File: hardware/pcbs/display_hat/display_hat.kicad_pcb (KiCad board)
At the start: 2 copper layers, 31 x 65 mm, 13 parts, among them J1 WAVESHARE_HAT_HEADER, J2 Header_01x08, J3 Header_01x08, J4 MTA100_02

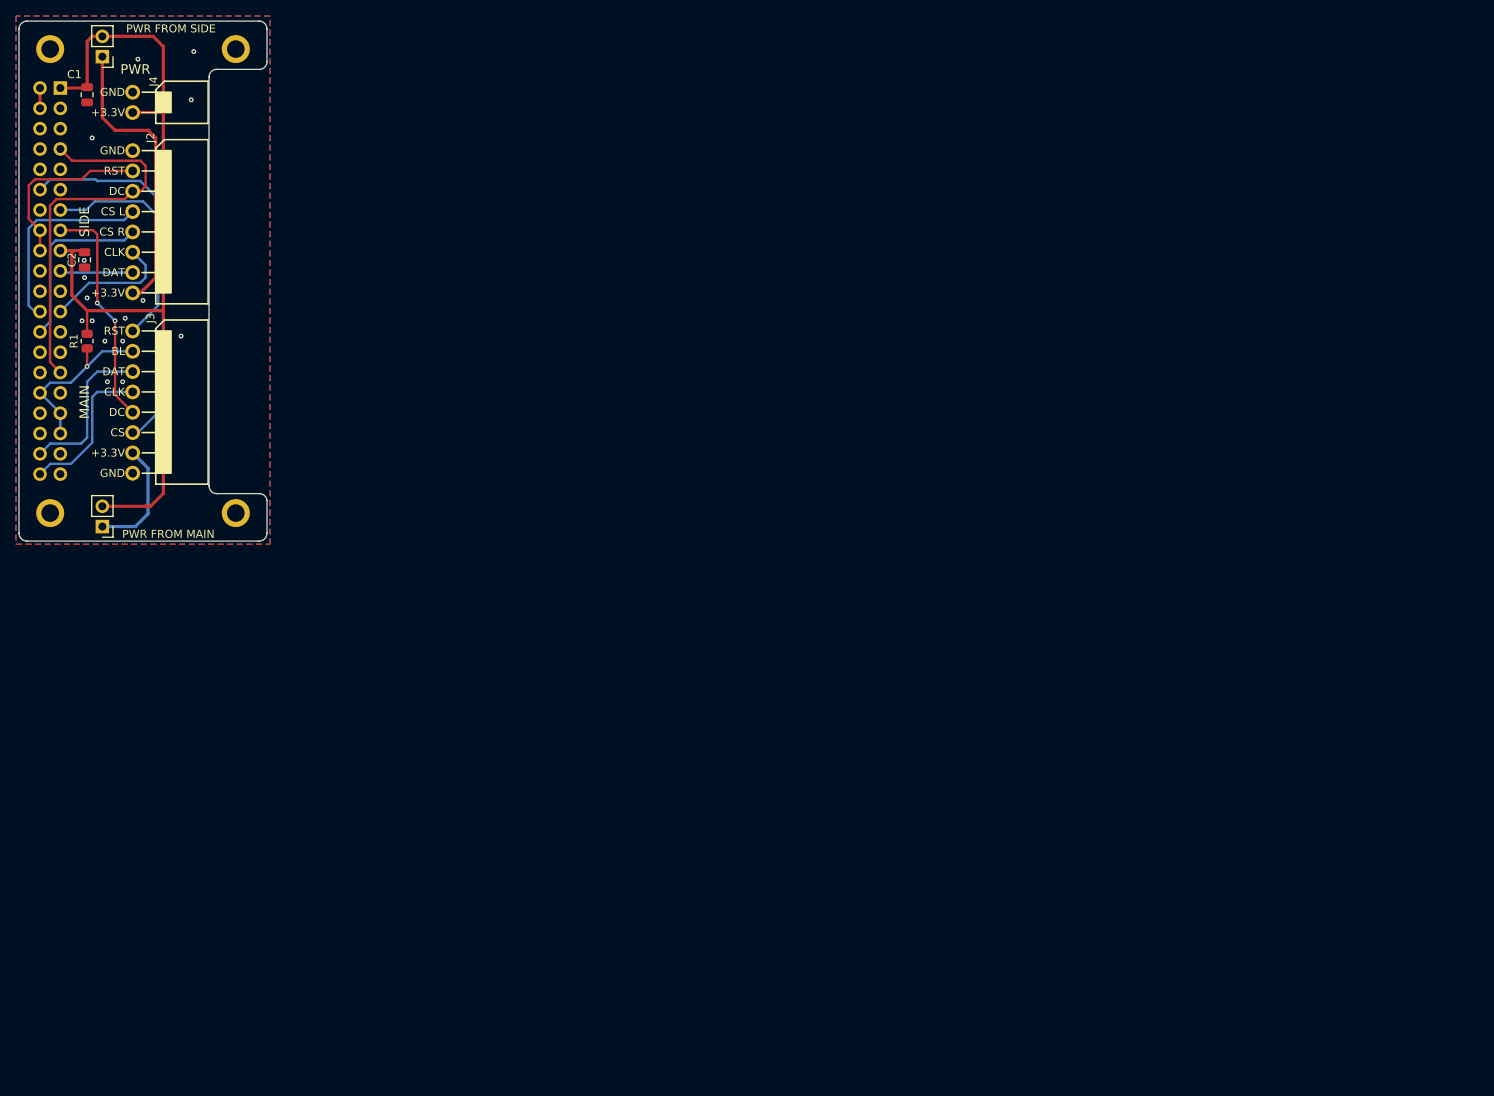
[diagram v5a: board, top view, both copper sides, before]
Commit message: boards: update fabrication output settings
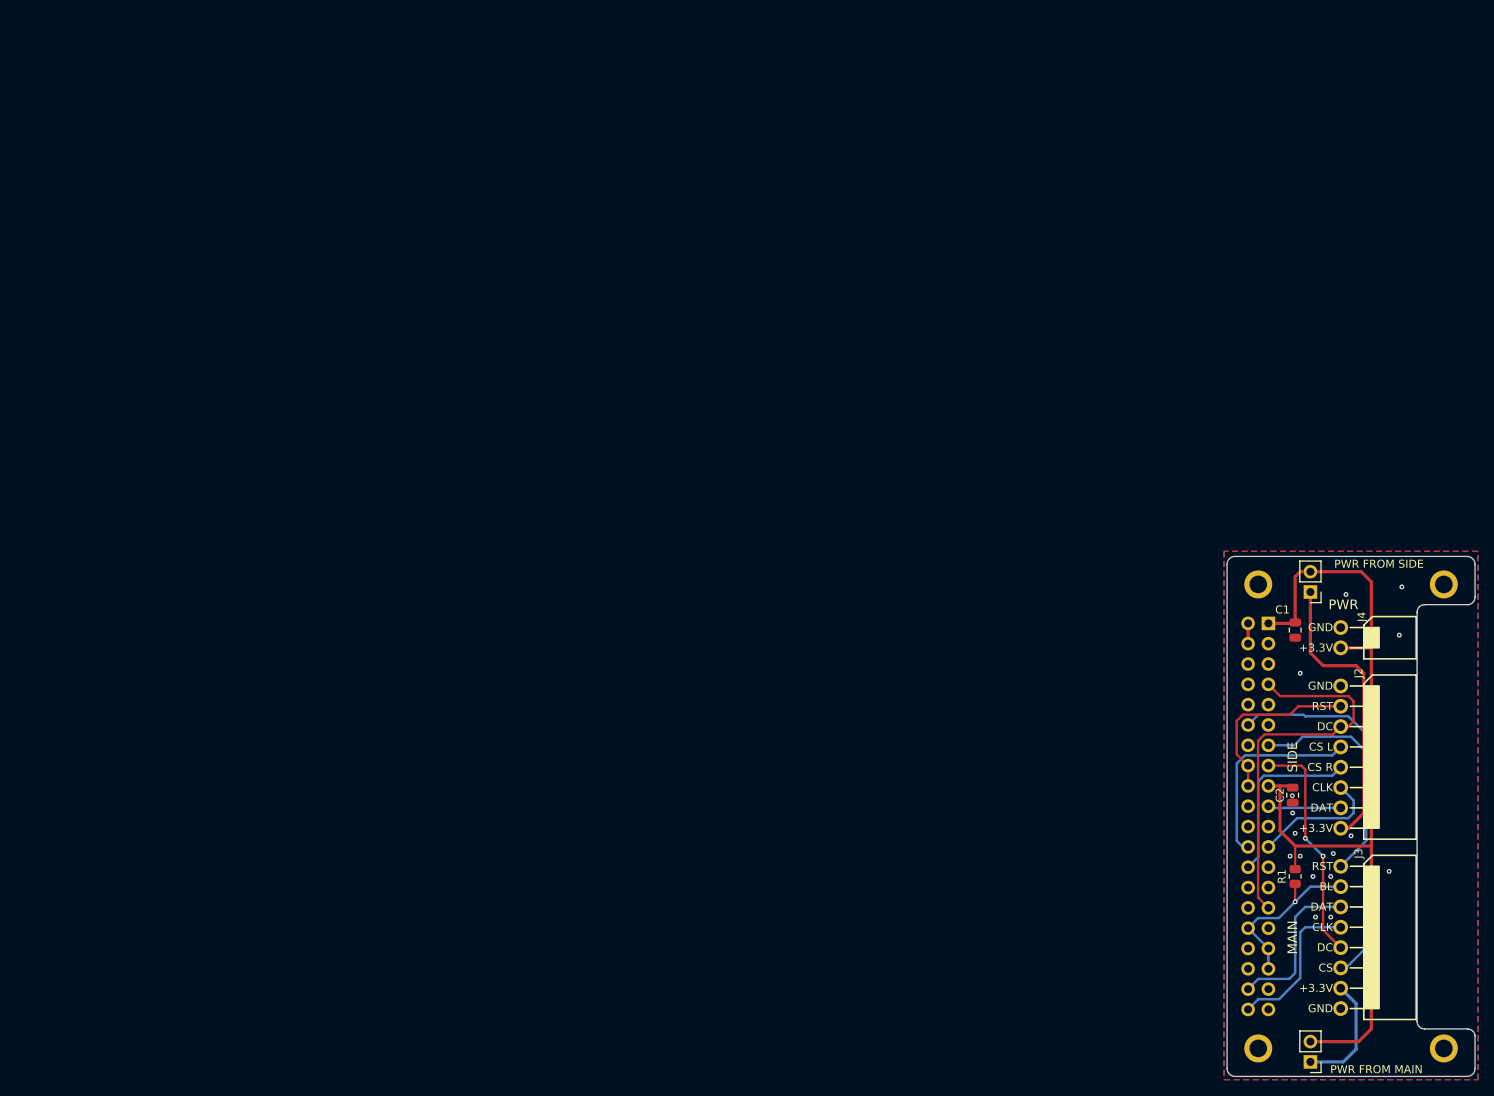
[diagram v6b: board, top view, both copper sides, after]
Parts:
- J2, J3: value Header_01x08 -> MTA100_08
- moved C1 165.2 mm to (144.0, 76.1)
- moved C2 165.2 mm to (143.7, 96.8)
- moved H2 165.2 mm to (139.4, 70.4)
- moved H3 165.2 mm to (162.6, 70.4)
- moved J1 165.2 mm to (140.7, 75.3)
- moved J2 165.2 mm to (149.7, 100.9)
- moved J3 165.2 mm to (149.7, 123.4)
- moved JP1 165.2 mm to (145.9, 71.4)
- moved JP2 165.2 mm to (145.9, 130.1)
- moved R1 165.2 mm to (144.0, 106.9)
- moved H1 165.2 mm to (162.6, 128.4)
- moved H4 165.2 mm to (139.4, 128.4)
- moved J4 165.2 mm to (149.7, 78.3)

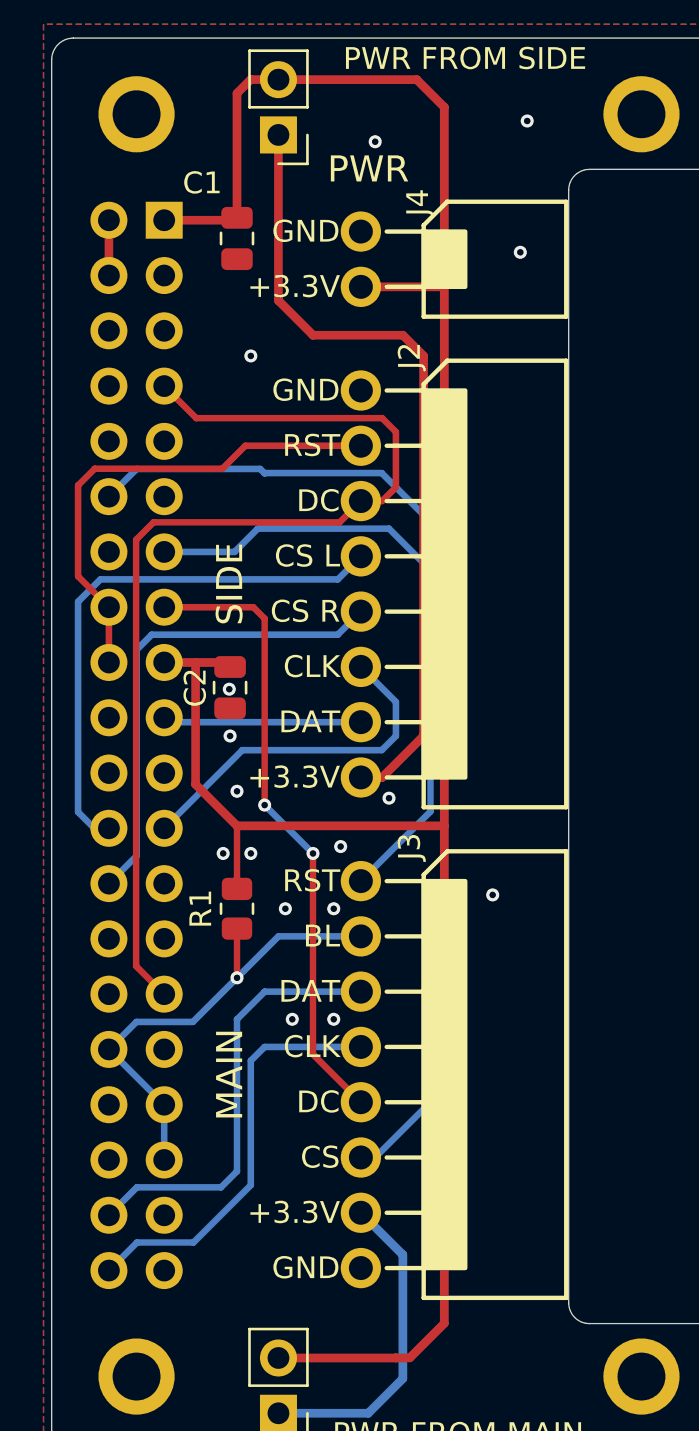
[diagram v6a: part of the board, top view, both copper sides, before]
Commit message: boards: fix many silly bugs discovered during testing
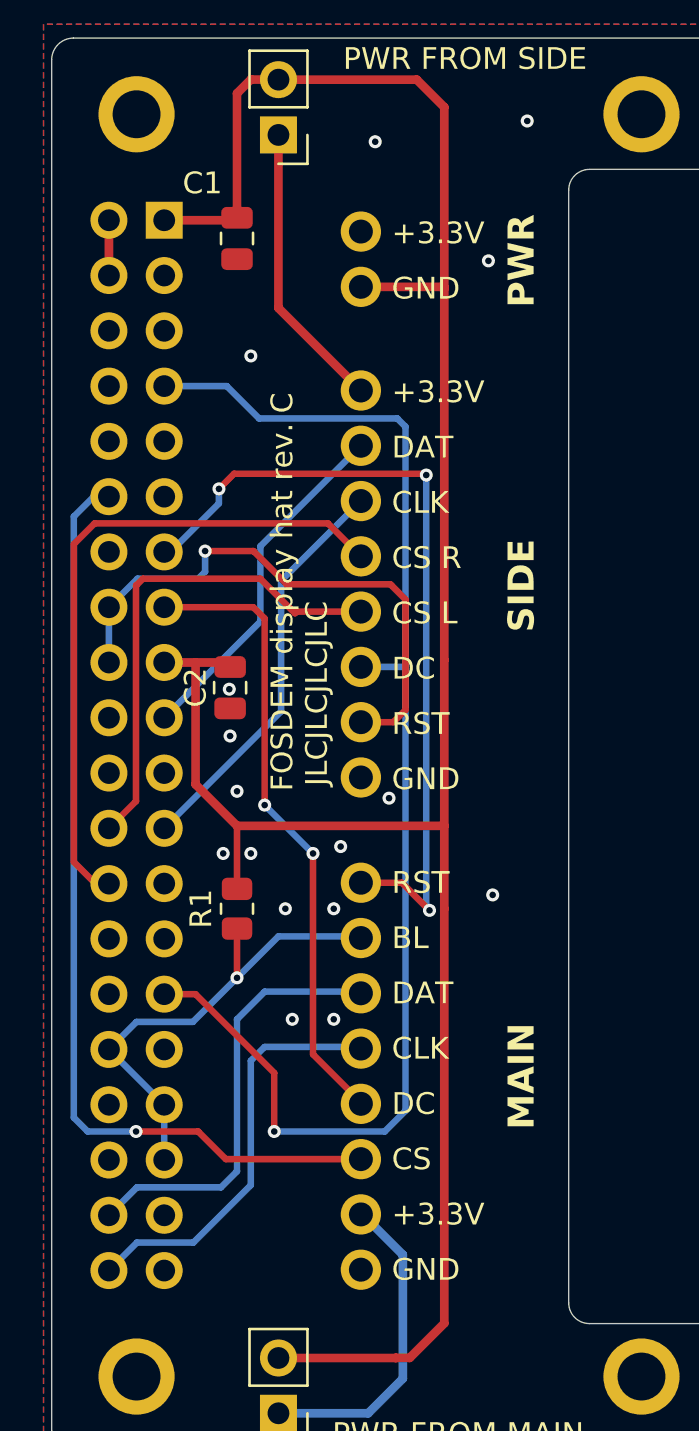
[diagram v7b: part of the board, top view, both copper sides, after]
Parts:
- J2, J3, J4: moved to B.Cu
- moved J2 17.8 mm to (149.7, 83.1), turned to -90 degrees
- moved J3 17.7 mm to (149.7, 105.7), turned to -90 degrees
- moved J4 2.54 mm to (149.7, 75.8), turned to -90 degrees
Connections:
- J3 pad 1: /MAIN_RST -> GND
- J3 pad 2: /BL -> Net-(J3-Pin_2)
- J3 pad 3: /MAIN_DAT -> /MAIN_CS
- J3 pad 4: /MAIN_CLK -> /MAIN_DC
- J3 pad 5: /MAIN_DC -> /MAIN_CLK
- J3 pad 6: /MAIN_CS -> /MAIN_DAT
- J3 pad 7: Net-(J3-Pin_7) -> /BL
- J3 pad 8: GND -> /MAIN_RST
- J4 pad 1: GND -> +3.3V
- J4 pad 2: +3.3V -> GND
- JP2 pad 1: Net-(J3-Pin_7) -> Net-(J3-Pin_2)
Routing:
- net Net-(J2-Pin_8): track 36.9 -> 13.3 mm
- net Net-(J3-Pin_7): track 14.9 -> 0.00 mm
- net Net-(J3-Pin_2): track 0.00 -> 14.9 mm
- net /SIDE_DC: track 48.4 -> 61.0 mm, vias 0 -> 1
- net /MAIN_RST: track 29.1 -> 37.7 mm, vias 0 -> 3
- net /SIDE_CS_R: track 22.3 -> 30.8 mm
- net /SIDE_DAT: track 9.12 -> 16.2 mm
- net /MAIN_CS: track 47.8 -> 43.6 mm, vias 0 -> 1
- net /SIDE_RST: track 22.5 -> 26.1 mm, vias 0 -> 1
- net /SIDE_CLK: track 16.2 -> 18.8 mm
- net /SIDE_CS_L: track 25.2 -> 22.8 mm
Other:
- board text added: "+3.3V"
- board text added: "BL"
- board text added: "CLK"
- board text added: "CS"
- board text added: "CS L"
- board text added: "CS R"
- board text added: "DAT"
- board text added: "DC"
- board text added: "FOSDEM display hat rev. C"
- board text added: "GND"
- board text added: "MAIN"
- board text added: "PWR"
- board text added: "RST"
- board text added: "SIDE"
- board text removed: "FOSDEM display hat rev. A"

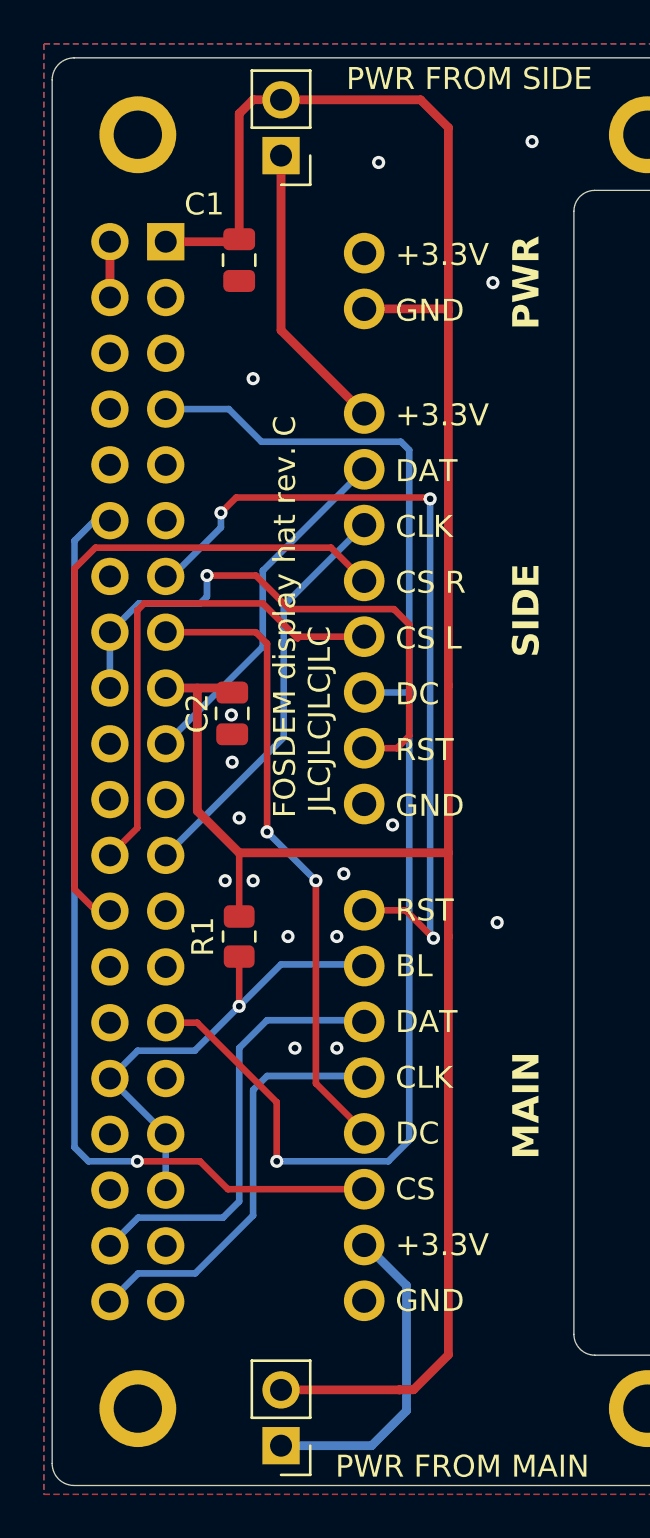
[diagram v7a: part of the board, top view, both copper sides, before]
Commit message: display_hat: fix pin order for main connector
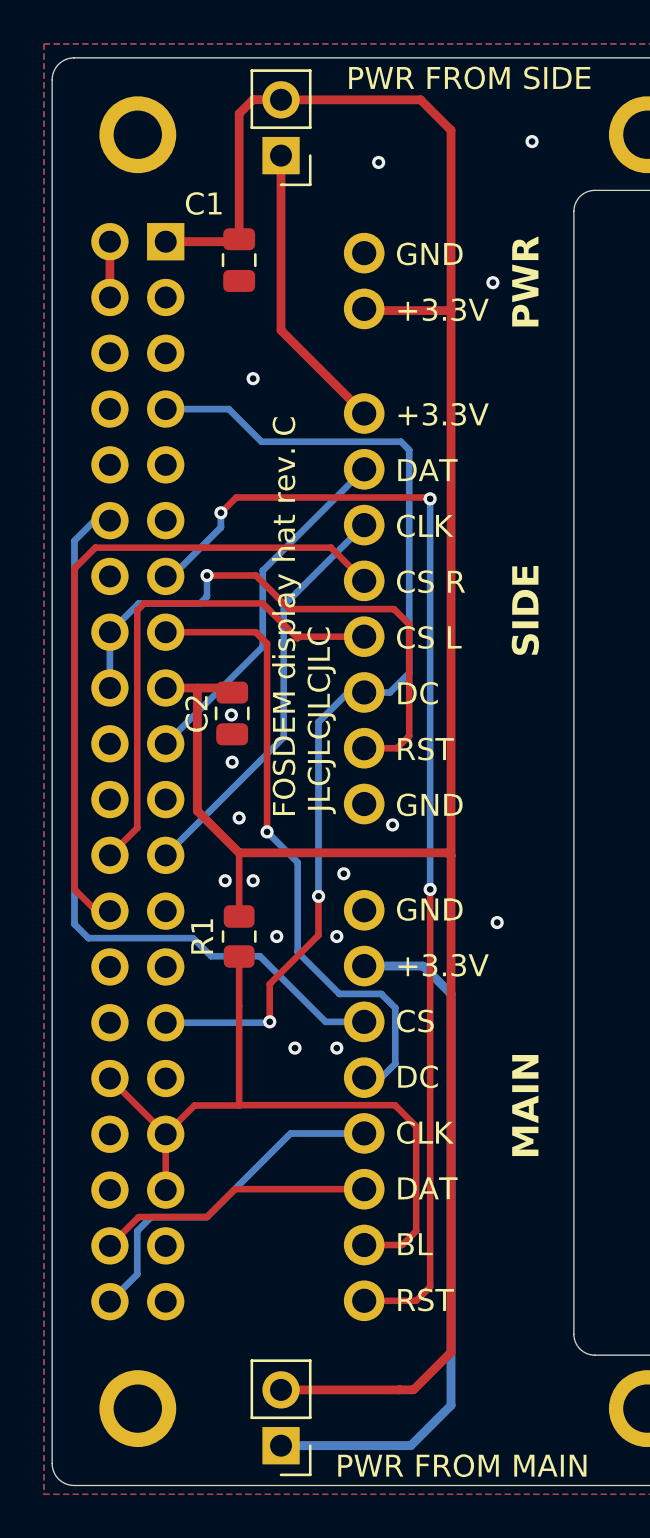
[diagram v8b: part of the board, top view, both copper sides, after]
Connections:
- J3 pad 1: GND -> /MAIN_RST
- J3 pad 2: Net-(J3-Pin_2) -> /BL
- J3 pad 3: /MAIN_CS -> /MAIN_DAT
- J3 pad 4: /MAIN_DC -> /MAIN_CLK
- J3 pad 5: /MAIN_CLK -> /MAIN_DC
- J3 pad 6: /MAIN_DAT -> /MAIN_CS
- J3 pad 7: /BL -> Net-(J3-Pin_7)
- J3 pad 8: /MAIN_RST -> GND
- JP2 pad 1: Net-(J3-Pin_2) -> Net-(J3-Pin_7)
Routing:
- net Net-(J3-Pin_7): track 0.00 -> 31.7 mm
- net /MAIN_RST: track 37.7 -> 53.1 mm
- net Net-(J3-Pin_2): track 14.9 -> 0.00 mm
- net /SIDE_DC: track 61.0 -> 46.4 mm, vias 1 -> 2
- net /BL: track 22.1 -> 32.7 mm, vias 1 -> 0
- net /MAIN_CS: track 43.6 -> 34.5 mm, vias 1 -> 0
- net /MAIN_DAT: track 19.9 -> 12.6 mm
- net /MAIN_CLK: track 19.2 -> 15.9 mm
- net /MAIN_DC: track 28.9 -> 29.2 mm, vias 2 -> 1
